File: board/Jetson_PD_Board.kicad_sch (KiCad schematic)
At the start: 37 parts, among them J1 USB4081-03-A, J2 768250002, Q1 NTTFS5C673NLTAG, Q2 NTTFS5C673NLTAG, Q3 NTTFS5C673NLTAG, U1 APK43070DKZ-13-FA01, U2 USBLC6-2SC6

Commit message: Updated schematic in accordance with design guide
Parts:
- added C11: 1nF, Capacitor_SMD:C_0603_1608Metric_Pad1.08x0.95mm_HandSolder, symbol Device:C
- added C12, C13: 10uF, Capacitor_SMD:C_1206_3216Metric_Pad1.33x1.80mm_HandSolder, symbol Device:C
- added C14: 0.1uF, Capacitor_SMD:C_0603_1608Metric_Pad1.08x0.95mm_HandSolder, symbol Device:C
- added D1: 1N4148WS, Diode_SMD:D_SOD-323, symbol Diode:1N4148WS
- added R13: 33k, Resistor_SMD:R_0603_1608Metric_Pad0.98x0.95mm_HandSolder, symbol Device:R_US
- added R14, R15, R16, R17: 22, Resistor_SMD:R_0603_1608Metric_Pad0.98x0.95mm_HandSolder, symbol Device:R_US
- C7, C8: value 15uF -> 1uF
- L1: value L -> 13uH
- R6, R7: value 100k -> 4.7k
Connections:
- net CC1: now also R16.2; no longer U1.2 (CC1)
- net CC2: now also R17.2; no longer U1.3 (CC2)
- net GND: now also C8.2, C11.2, C12.2, C13.2, C14.2; no longer C8.1
- net V_{batt}: now also C12.1, C13.1, C14.1
- net at C1.1, C2.1, L1.2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: now also D1.2 (A)
- net at U1.19 (GATE): now also R13.1; no longer Q3.2 (G)
- net at U1.20 (VDRV): now also C8.1; no longer C8.2
- net at U1.4 (DN): now also R15.1; no longer U2.3 (I/O2)
- net at U1.5 (DP): now also R14.1; no longer U2.1 (I/O1)
- net at TH1.1, U1.6 (TS): now also C11.1
- new net: R16.1, U1.2 (CC1)
- new net: R17.1, U1.3 (CC2)
- new net: D1.1 (K), Q3.2 (G), R13.2
- new net: R14.2, U2.1 (I/O1)
- new net: R15.2, U2.3 (I/O2)
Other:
- moved on the sheet: D5, J2, Q3, R1, R10, R12, R8, R9, TH1

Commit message: Placed most components
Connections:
- net DP: now reaches R14.2, U2.1 (I/O1)
- net DN: now reaches R15.2, U2.3 (I/O2)
- net USB_DN: now reaches J1.B7 (DN2), U2.4 (I/O2)
- net USB_DP: now reaches J1.B6 (DP2), U2.6 (I/O1)
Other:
- moved on the sheet: D4, R11
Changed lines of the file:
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@@
 	(wire
 		(pts
-			(xy 217.17 69.85) (xy 220.98 69.85)
+			(xy 213.36 53.34) (xy 217.17 53.34)
 		)
 		(stroke
@@
 	(wire
 		(pts
-			(xy 228.6 69.85) (xy 234.95 69.85)
+			(xy 224.79 53.34) (xy 231.14 53.34)
 		)
 		(stroke
@@
 	(wire
 		(pts
-			(xy 205.74 69.85) (xy 209.55 69.85)
+			(xy 201.93 53.34) (xy 205.74 53.34)
 		)
 		(stroke
@@
 	(wire
 		(pts
-			(xy 205.74 69.85) (xy 205.74 67.31)
+			(xy 201.93 53.34) (xy 201.93 50.8)
 		)
 		(stroke
@@
 		)
 	)
+	(label "USB_DN"
+		(at 237.49 139.7 0)
+		(effects
+			(font
+				(size 1.27 1.27)
+			)
+			(justify left bottom)
+		)
+	)
 	(label "Switching_Node"
 		(at 129.54 85.09 0)
@@
 		)
 	)
+	(label "USB_DP"
+		(at 237.49 137.16 0)
+		(effects
+			(font
+				(size 1.27 1.27)
+			)
+			(justify left bottom)
+		)
+	)
+	(label "DP"
+		(at 168.91 137.16 0)
+		(effects
+			(font
+				(size 1.27 1.27)
+			)
+			(justify left bottom)
+		)
+	)
+	(label "DN"
+		(at 168.91 139.7 0)
+		(effects
+			(font
+				(size 1.27 1.27)
+			)
+			(justify left bottom)
+		)
+	)
 	(global_label "CC1"
 		(shape bidirectional)
@@
 	(symbol
 		(lib_id "Device:LED")
-		(at 224.79 69.85 180)
+		(at 220.98 53.34 180)
 		(unit 1)
 		(exclude_from_sim no)
@@
 		(dnp no)
 		(property "Reference" "D4"
-			(at 223.266 66.802 0)
+			(at 219.456 50.292 0)
 			(effects
 				(font
@@
 		)
 		(property "Value" "LED (Blue)"
-			(at 219.71 73.152 0)
+			(at 215.9 56.642 0)
 			(effects
 				(font
@@
 		)
 		(property "Footprint" "LED_SMD:LED_0603_1608Metric"
-			(at 224.79 69.85 0)
+			(at 220.98 53.34 0)
 			(effects
 				(font
@@
 		)
 		(property "Datasheet" "~"
-			(at 224.79 69.85 0)
+			(at 220.98 53.34 0)
 			(effects
 				(font
@@
 		)
 		(property "Description" "+10V Indicator"
-			(at 224.79 69.85 0)
+			(at 220.98 53.34 0)
 			(effects
 				(font
@@
 		)
 		(property "Sim.Pins" "1=K 2=A"
-			(at 224.79 69.85 0)
+			(at 220.98 53.34 0)
 			(effects
 				(font
@@
 	(symbol
 		(lib_id "power:+24V")
-		(at 205.74 67.31 0)
+		(at 201.93 50.8 0)
 		(mirror y)
 		(unit 1)
@@
 		(dnp no)
 		(property "Reference" "#PWR026"
-			(at 205.74 71.12 0)
+			(at 201.93 54.61 0)
 			(effects
 				(font
@@
 		)
 		(property "Value" "V_{out}"
-			(at 205.74 63.246 0)
+			(at 201.93 46.736 0)
 			(effects
 				(font
@@
 		)
 		(property "Footprint" ""
-			(at 205.74 67.31 0)
+			(at 201.93 50.8 0)
 			(effects
 				(font
@@
 		)
 		(property "Datasheet" ""
-			(at 205.74 67.31 0)
+			(at 201.93 50.8 0)
 			(effects
 				(font
@@
 		)
 		(property "Description" "Power symbol creates a global label with name \"+24V\""
-			(at 205.74 67.31 0)
+			(at 201.93 50.8 0)
 			(effects
 				(font
@@
 	(symbol
 		(lib_id "Device:R_US")
-		(at 213.36 69.85 90)
+		(at 209.55 53.34 90)
 		(unit 1)
 		(exclude_from_sim no)
@@
 		(dnp no)
 		(property "Reference" "R11"
-			(at 215.138 67.31 90)
+			(at 211.328 50.8 90)
 			(effects
 				(font
@@
 		)
 		(property "Value" "820"
-			(at 215.138 72.644 90)
+			(at 211.328 56.134 90)
 			(effects
 				(font
@@
 		)
 		(property "Footprint" "Resistor_SMD:R_0603_1608Metric_Pad0.98x0.95mm_HandSolder"
-			(at 213.614 68.834 90)
+			(at 209.804 52.324 90)
 			(effects
 				(font
@@
 		)
 		(property "Datasheet" "~"
-			(at 213.36 69.85 0)
+			(at 209.55 53.34 0)
 			(effects
 				(font
@@
 		)
 		(property "Description" "Resistor, US symbol"
-			(at 213.36 69.85 0)
+			(at 209.55 53.34 0)
 			(effects
 				(font
@@
 	(symbol
 		(lib_id "power:GND")
-		(at 234.95 69.85 0)
+		(at 231.14 53.34 0)
 		(mirror y)
 		(unit 1)
@@
 		(dnp no)
 		(property "Reference" "#PWR025"
-			(at 234.95 76.2 0)
+			(at 231.14 59.69 0)
 			(effects
 				(font
@@
 		)
 		(property "Value" "GND"
-			(at 234.95 73.66 0)
+			(at 231.14 57.15 0)
 			(effects
 				(font
@@
 		)
 		(property "Footprint" ""
-			(at 234.95 69.85 0)
+			(at 231.14 53.34 0)
 			(effects
 				(font
@@
 		)
 		(property "Datasheet" ""
-			(at 234.95 69.85 0)
+			(at 231.14 53.34 0)
 			(effects
 				(font
@@
 		)
 		(property "Description" "Power symbol creates a global label with name \"GND\" , ground"
-			(at 234.95 69.85 0)
+			(at 231.14 53.34 0)
 			(effects
 				(font

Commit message: Reviewed first placement and ordered signals on back
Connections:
- net V_{out}: no longer R6.1, R7.1
- net V5V: now reaches C7.1, U1.21 (V5V)
- net V5V: now also R6.1, R7.1
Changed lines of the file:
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@@
 	)
 	(junction
+		(at 101.6 86.36)
+		(diameter 0)
+		(color 0 0 0 0)
+	)
+	(junction
 		(at 40.64 82.55)
 		(diameter 0)
@@
 	(wire
 		(pts
-			(xy 101.6 83.82) (xy 101.6 87.63)
+			(xy 101.6 83.82) (xy 101.6 86.36)
 		)
 		(stroke
@@
 	(wire
 		(pts
+			(xy 101.6 86.36) (xy 101.6 87.63)
+		)
+		(stroke
+			(width 0)
+			(type default)
+		)
+	)
+	(wire
+		(pts
 			(xy 109.22 133.35) (xy 115.57 133.35)
 		)
@@
 	(wire
 		(pts
+			(xy 106.68 76.2) (xy 106.68 86.36)
+		)
+		(stroke
+			(width 0)
+			(type default)
+		)
+	)
+	(wire
+		(pts
 			(xy 189.23 109.22) (xy 189.23 111.76)
 		)
@@
 	(wire
 		(pts
+			(xy 106.68 86.36) (xy 101.6 86.36)
+		)
+		(stroke
+			(width 0)
+			(type default)
+		)
+	)
+	(wire
+		(pts
 			(xy 222.25 97.79) (xy 238.76 97.79)
 		)
@@
 	)
 	(symbol
+		(lib_id "power:+24V")
+		(at 106.68 76.2 0)
+		(unit 1)
+		(exclude_from_sim no)
+		(in_bom yes)
+		(on_board yes)
+		(dnp no)
+		(property "Reference" "#PWR029"
+			(at 106.68 80.01 0)
+			(effects
+				(font
+					(size 1.27 1.27)
+				)
+				(hide yes)
+			)
+		)
+		(property "Value" "V5V"
+			(at 106.68 72.136 0)
+			(effects
+				(font
+					(size 1.27 1.27)
+				)
+			)
+		)
+		(property "Footprint" ""
+			(at 106.68 76.2 0)
+			(effects
+				(font
+					(size 1.27 1.27)
+				)
+				(hide yes)
+			)
+		)
+		(property "Datasheet" ""
+			(at 106.68 76.2 0)
+			(effects
+				(font
+					(size 1.27 1.27)
+				)
+				(hide yes)
+			)
+		)
+		(property "Description" "Power symbol creates a global label with name \"+24V\""
+			(at 106.68 76.2 0)
+			(effects
+				(font
+					(size 1.27 1.27)
+				)
+				(hide yes)
+			)
+		)
+		(pin "1"
+		)
+		(instances
+			(project "Jetson_PD_Board"
+				(path "/fbd9c71c-f200-4aab-a303-9f269bc9de13"
+					(reference "#PWR029")
+					(unit 1)
+				)
+			)
+		)
+	)
+	(symbol
 		(lib_id "Device:C")
 		(at 44.45 77.47 0)
@@
 			)
 		)
-		(property "Value" "V_{out}"
+		(property "Value" "V5V"
 			(at 66.04 110.236 0)
 			(effects

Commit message: aaaaaaaaaaaaaaaaaaaaaaaaA
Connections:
- net Buck_{out}: now reaches C1.1, C2.1, D1.2 (A), L1.2, Q3.3 (S), R5.1, U1.24 (CSP)
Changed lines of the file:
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@@
+		)
+	)
+	(label "Buck_{out}"
+		(at 162.56 54.61 0)
+		(effects
+			(font
+				(size 1.27 1.27)
+			)
+			(justify left bottom)
 		)
 	)

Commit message: Connected USB-C shield to GND
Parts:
- J1: footprint PD_Hardware_Footprints:CONN24_USB4081_GCT -> CONN24_USB4081_GCT
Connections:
- net GND: now also J1.SH
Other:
- moved on the sheet: C1, C10, C11, C12, C13, C14, C2, C3, C4, C5, C6, C7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

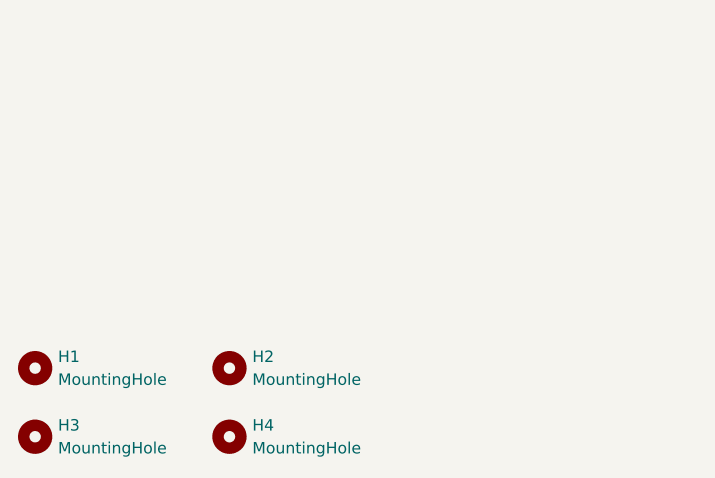
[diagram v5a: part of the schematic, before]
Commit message: Grounded mounting holes
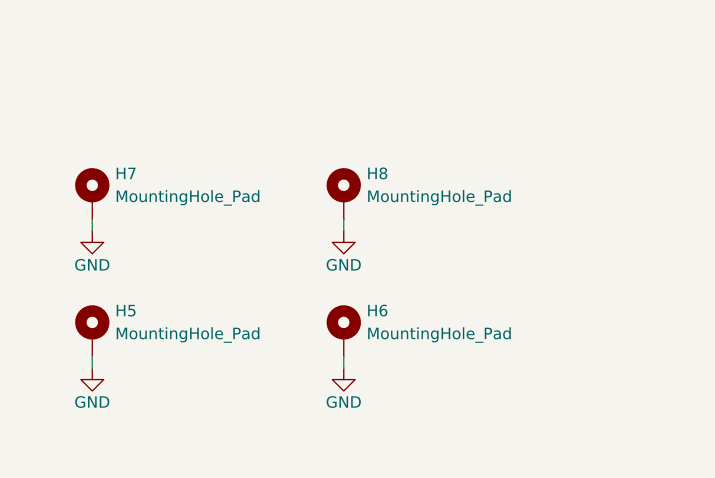
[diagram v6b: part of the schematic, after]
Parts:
- removed H1, H2, H3, H4: MountingHole, MountingHole:MountingHole_3.2mm_M3_ISO14580_Pad_TopBottom, symbol Mechanical:MountingHole
- added H5, H6, H7, H8: MountingHole_Pad, MountingHole:MountingHole_3.2mm_M3_ISO14580_Pad_TopBottom, symbol Mechanical:MountingHole_Pad
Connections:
- net GND: now also H5.1, H6.1, H7.1, H8.1

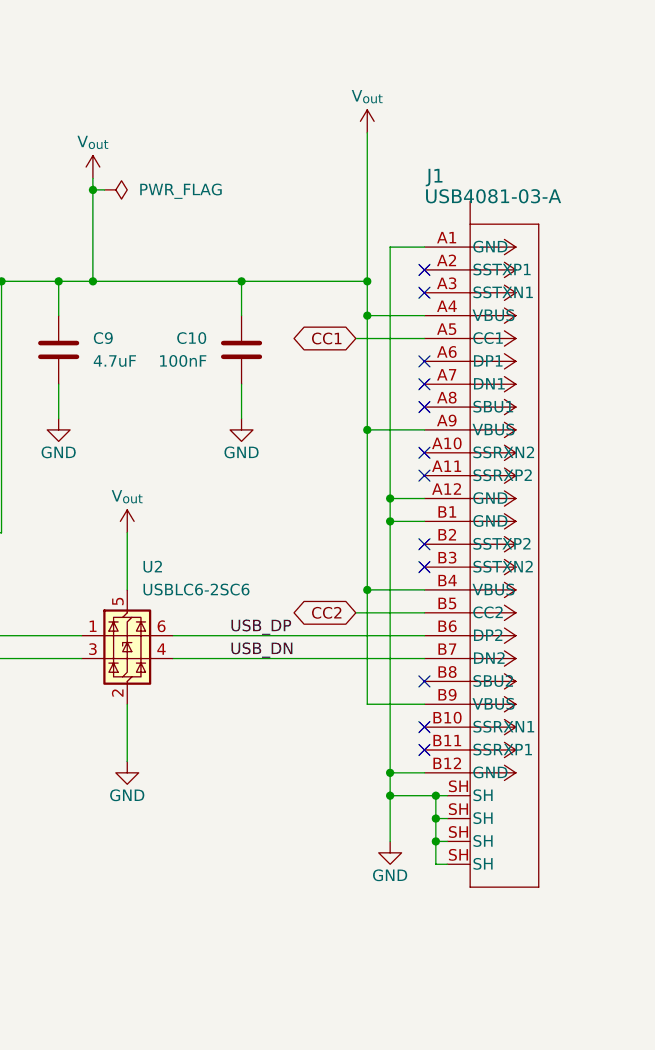
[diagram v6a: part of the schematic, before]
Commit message: Updated design to ordered state.
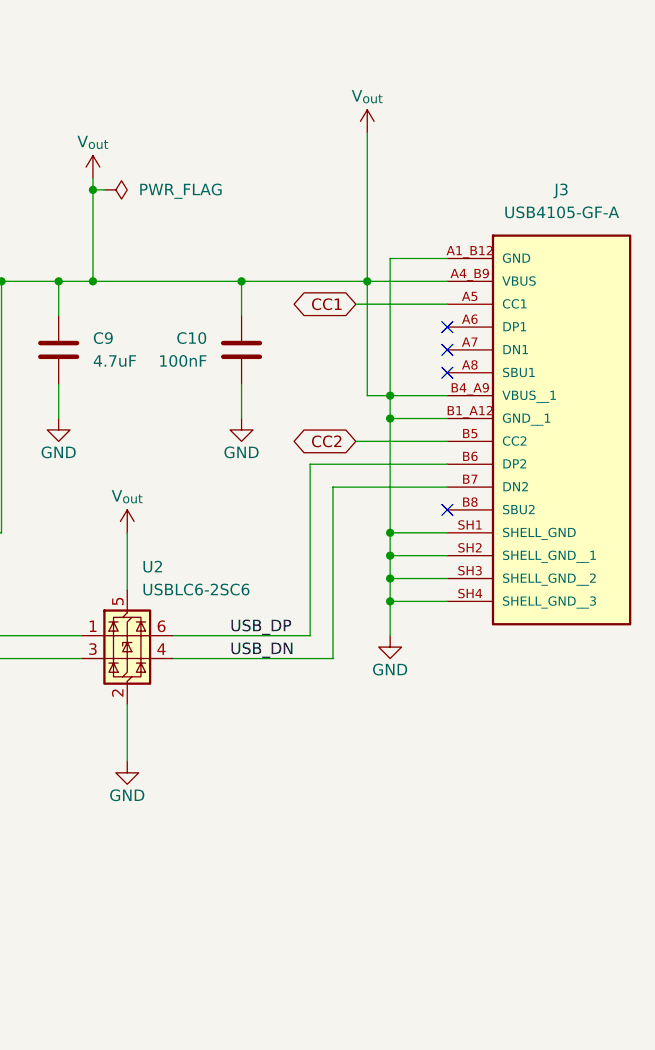
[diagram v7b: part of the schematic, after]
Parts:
- removed J1: USB4081-03-A, CONN24_USB4081_GCT, symbol PD_Control_Hardware:USB4081-03-A
- added J3: USB4105-GF-A, MRDT_Connectors:GCT_USB4105-GF-A, symbol MRDT_Connectors:USB4105-GF-A
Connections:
- net V_{out} is gone; now on net GND: C10.1, C9.1, R11.1, R3.2, R5.2, U1.23 (CSN), U2.5 (VBUS)
- net CC1: now also J3.A5 (CC1)
- net CC2: now also J3.B5 (CC2)
- net GND: now also J3.A1_B12 (GND), J3.A4_B9 (VBUS), J3.B1_A12 (GND__1), J3.B4_A9 (VBUS__1), J3.SH1 (SHELL_GND), J3.SH2 (SHELL_GND__1), J3.SH3 (SHELL_GND__2), J3.SH4 (SHELL_GND__3)
- net USB_DN: now also J3.B7 (DN2)
- net USB_DP: now also J3.B6 (DP2)
- no-connect marks 13 -> 5

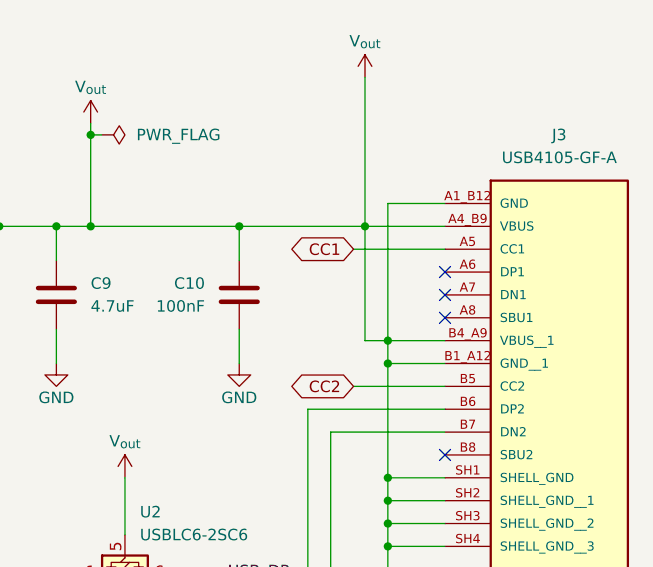
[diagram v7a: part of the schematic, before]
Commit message: Fix Vbus shorted to GND
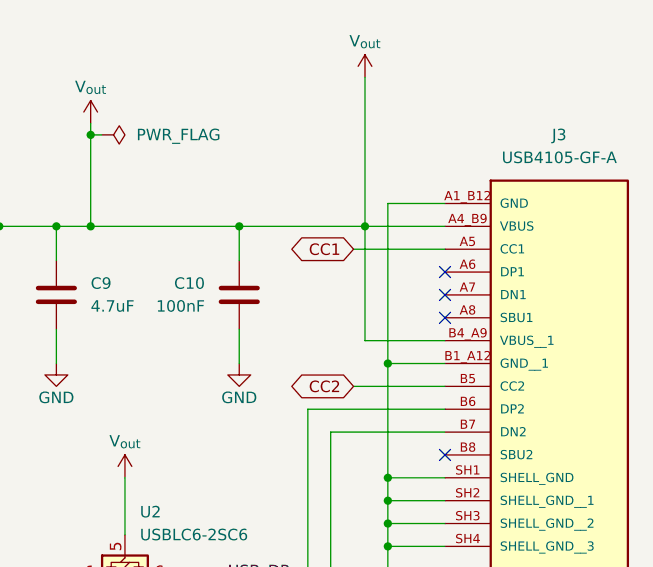
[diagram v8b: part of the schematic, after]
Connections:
- net GND: no longer C10.1, C9.1, J3.A4_B9 (VBUS), J3.B4_A9 (VBUS__1), R11.1, R3.2, R5.2, U1.23 (CSN), U2.5 (VBUS)
- new net V_{out}: C10.1, C9.1, J3.A4_B9 (VBUS), J3.B4_A9 (VBUS__1), R11.1, R3.2, R5.2, U1.23 (CSN), U2.5 (VBUS)
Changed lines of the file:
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@@
-	)
-	(junction
-		(at 254 99.06)
-		(diameter 0)
-		(color 0 0 0 0)
 	)
 	(junction
@@
 	(wire
 		(pts
-			(xy 254 99.06) (xy 254 101.6)
-		)
-		(stroke
-			(width 0)
-			(type default)
-		)
-	)
-	(wire
-		(pts
 			(xy 63.5 81.28) (xy 66.04 81.28)
 		)
@@
 	(wire
 		(pts
-			(xy 254 83.82) (xy 254 99.06)
-		)
-		(stroke
-			(width 0)
-			(type default)
-		)
-	)
-	(wire
-		(pts
 			(xy 82.55 130.81) (xy 82.55 129.54)
 		)
@@
 	(wire
 		(pts
+			(xy 254 83.82) (xy 254 101.6)
+		)
+		(stroke
+			(width 0)
+			(type default)
+		)
+	)
+	(wire
+		(pts
 			(xy 100.33 128.27) (xy 100.33 109.22)
 		)
@@
 	(wire
 		(pts
+			(xy 251.46 99.06) (xy 260.35 99.06)
+		)
+		(stroke
+			(width 0)
+			(type default)
+		)
+	)
+	(wire
+		(pts
 			(xy 27.94 101.6) (xy 25.4 101.6)
 		)
@@
 	(wire
 		(pts
-			(xy 254 99.06) (xy 260.35 99.06)
-		)
-		(stroke
-			(width 0)
-			(type default)
-		)
-	)
-	(wire
-		(pts
 			(xy 180.34 86.36) (xy 187.96 86.36)
 		)
@@
 		)
 		(stroke
-			(width 0)
-			(type default)
-		)
-	)
-	(wire
-		(pts
-			(xy 251.46 99.06) (xy 254 99.06)
-		)
-		(stroke
